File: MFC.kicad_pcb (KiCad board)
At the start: 2 copper layers, 101.6 x 53.3 mm, 39 parts, among them J1 DA15_Receptacle_MountingHoles, J12 Conn_01x01_Pin, J2 Conn_01x04_Pin, J3 Conn_01x03_Socket, J4 647676-3, J5 Conn_01x03_Pin, J6 Conn_01x03_Pin, U1 MAX232

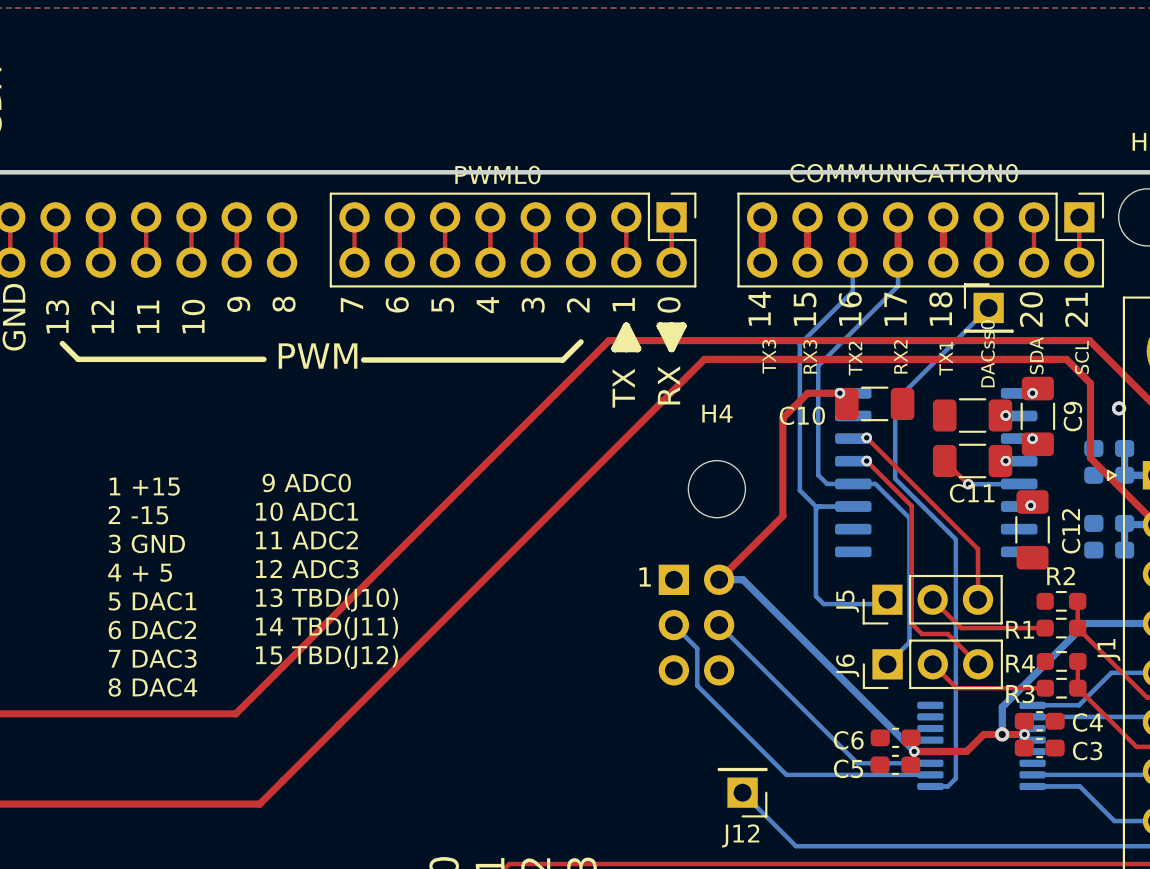
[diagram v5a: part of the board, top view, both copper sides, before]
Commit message: Added choice for serial com
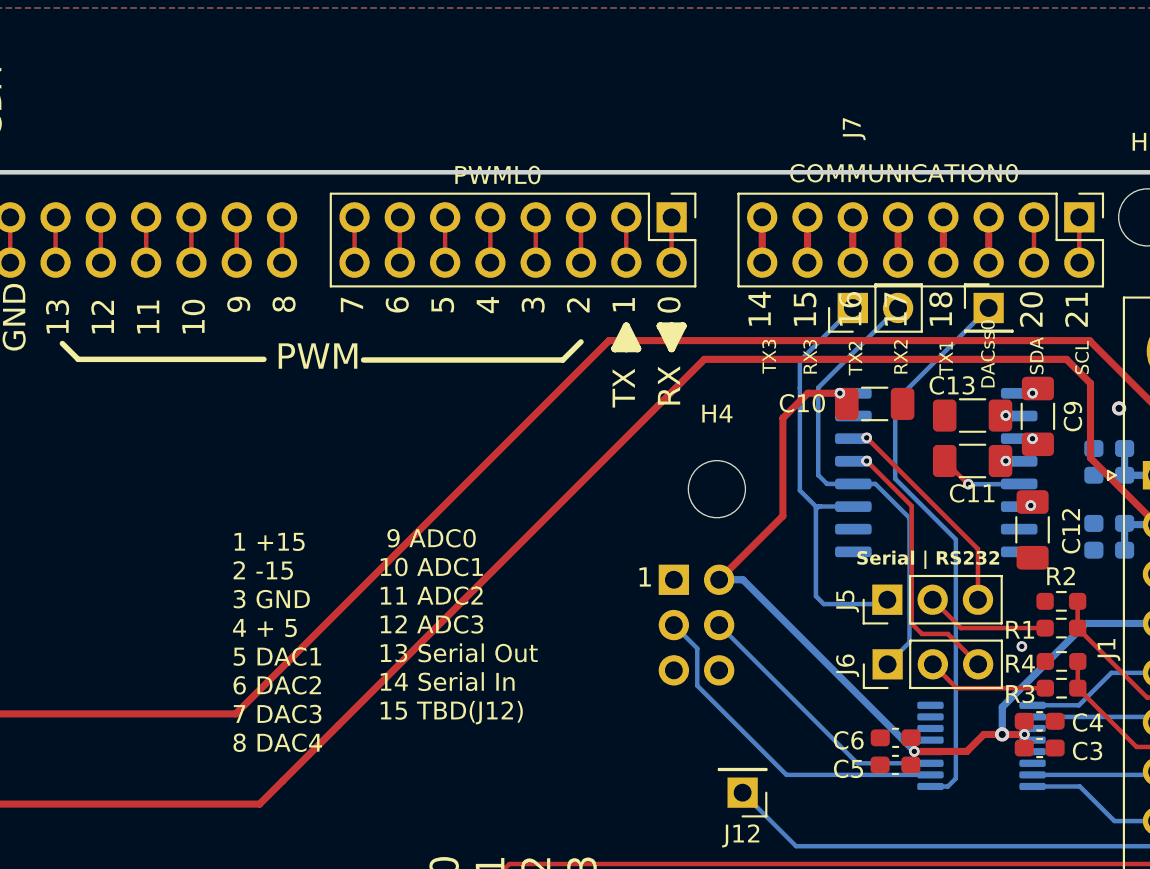
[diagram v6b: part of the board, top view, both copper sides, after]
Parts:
- added J7: Conn_01x02_Pin, Connector_PinHeader_2.54mm:PinHeader_1x02_P2.54mm_Vertical, F.Cu at (160.7, 76.8)
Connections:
- J5 pad 1: /TXD2 -> /TX2
- J6 pad 1: /RXD2 -> /RX2
- U1 pad 11: /TXD2 -> /TX2
- U1 pad 12: /RXD2 -> /RX2
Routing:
- net /RXD2: track 31.1 -> 2.54 mm
- net /TXD2: track 29.5 -> 2.54 mm
- net /RX2: track 0.00 -> 26.1 mm
- net /TX2: track 0.00 -> 24.5 mm
- net GND: vias 3 -> 4
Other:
- board text added: "9 ADC0 10 ADC1 11 ADC2 12 ADC3 13 Serial Out 14 Serial In 15 TBD(J12)"
- board text added: "Serial | RS232"
- board text removed: "9 ADC0 10 ADC1 11 ADC2 12 ADC3 13 TBD(J10) 14 TBD(J11) 15 TBD(J12)"

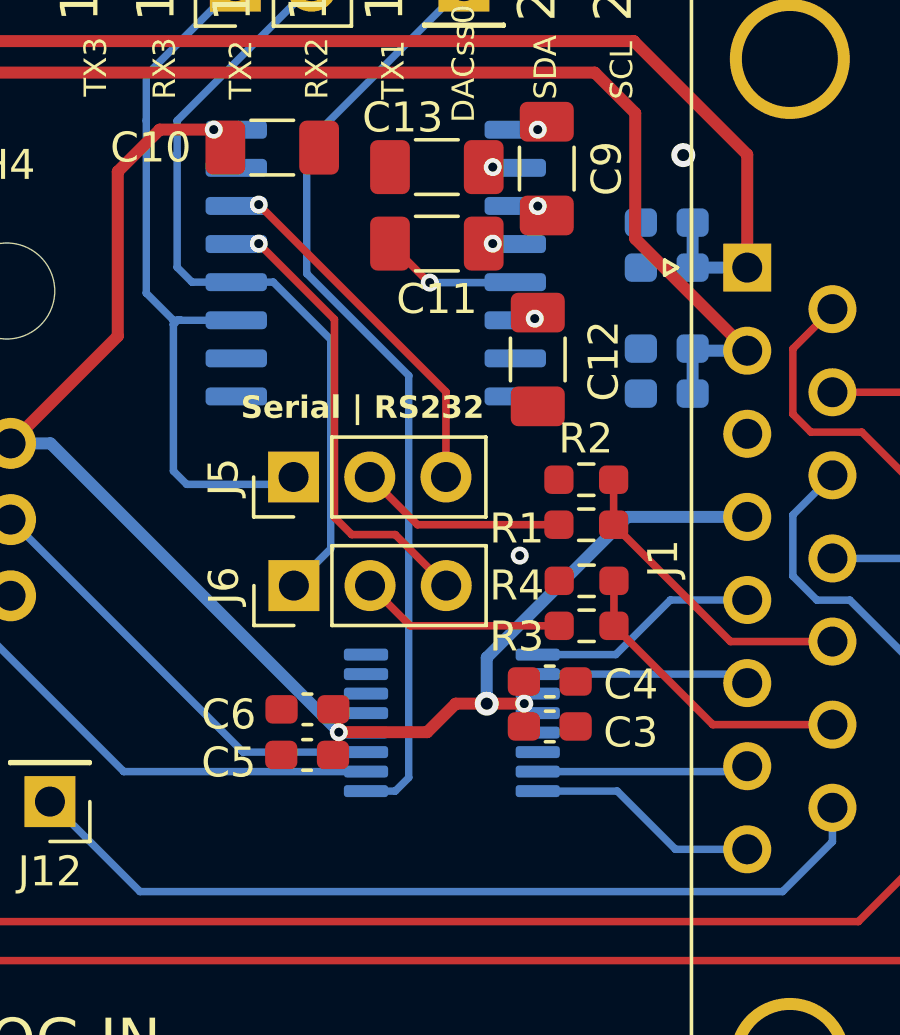
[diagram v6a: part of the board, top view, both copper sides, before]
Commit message: Update 10u capa for tantal
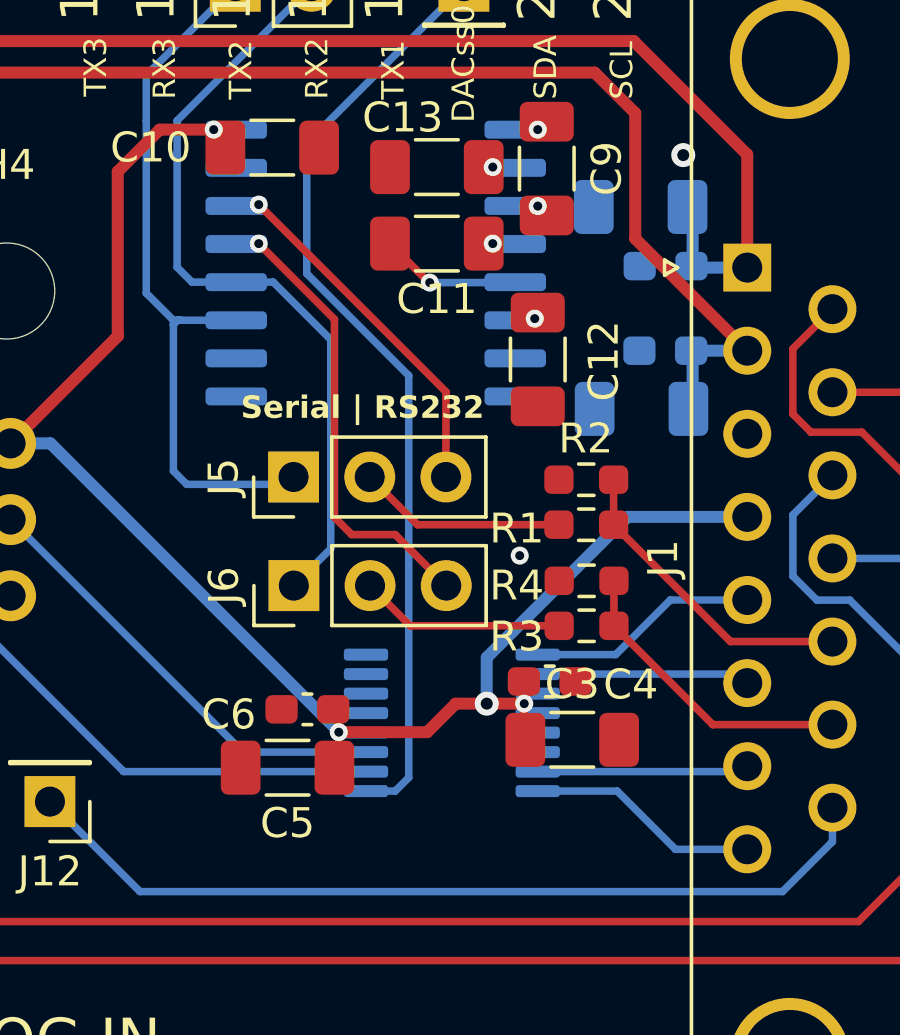
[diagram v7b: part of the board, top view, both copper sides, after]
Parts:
- C1, C3, C5, C7: footprint Capacitor_SMD:C_0603_1608Metric_Pad1.08x0.95mm_HandSolder -> Capacitor_SMD:C_1206_3216Metric_Pad1.33x1.80mm_HandSolder
- moved C1 2.20 mm to (174.2, 84.2)
- moved C7 2.18 mm to (174.3, 90.9)
- moved C2 1.45 mm to (175.1, 86.2)
- moved C8 1.43 mm to (175.1, 89.0)
- moved C3 0.87 mm to (171.9, 101.9)
- moved C5 0.78 mm to (162.5, 102.9)

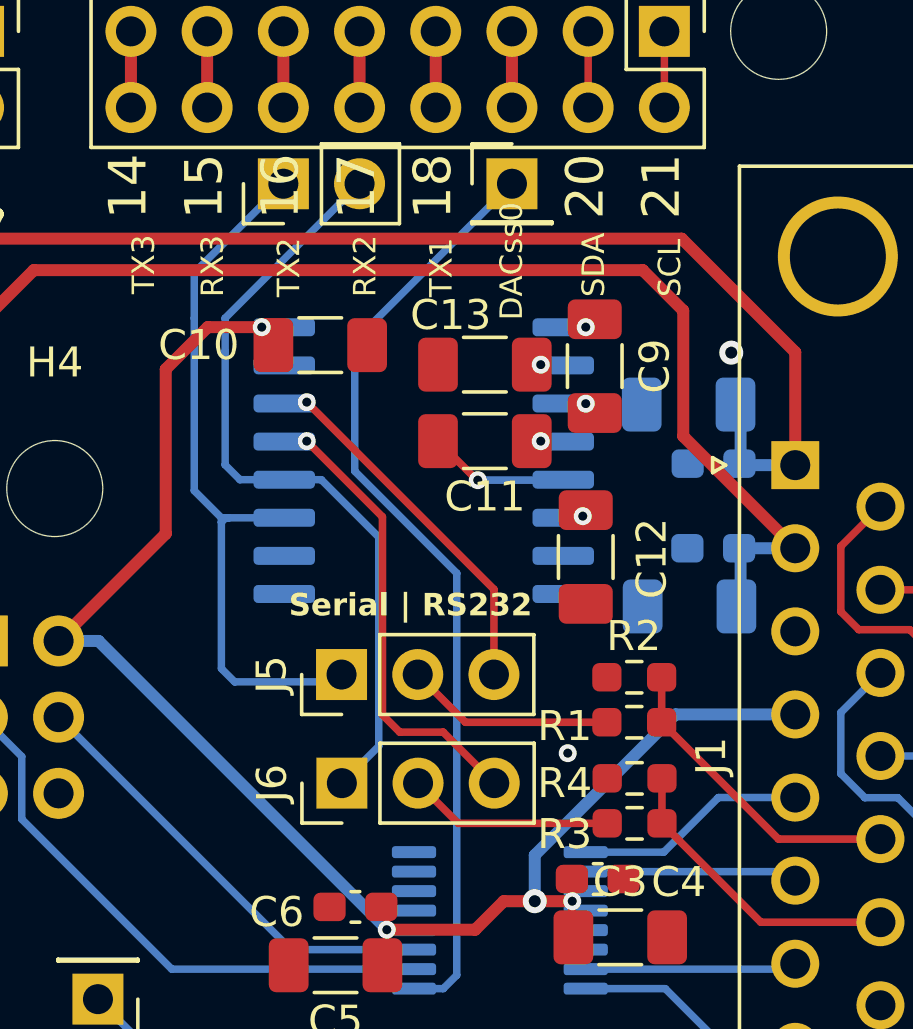
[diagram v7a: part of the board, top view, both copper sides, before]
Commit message: Minor change for better ground coverage
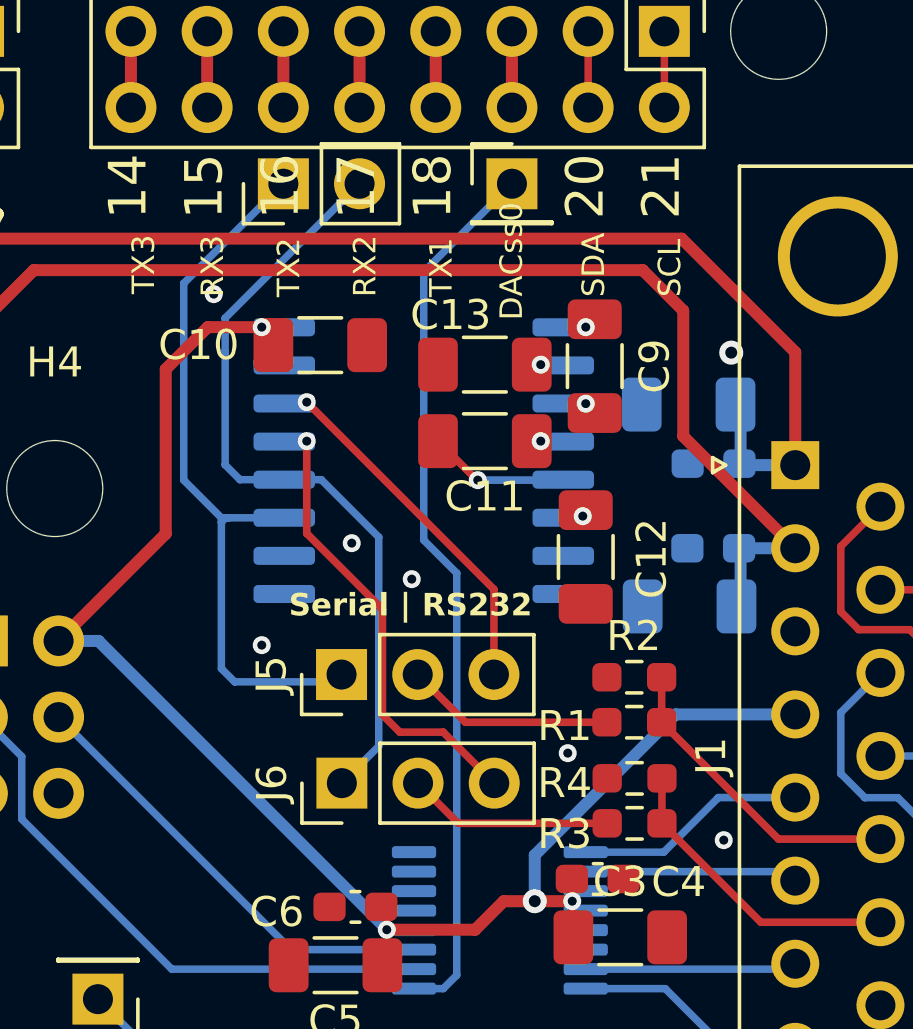
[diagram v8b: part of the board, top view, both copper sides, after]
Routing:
- net /SS: track 31.6 -> 29.7 mm
- net GND: vias 4 -> 9
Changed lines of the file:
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@@
   )
   (segment (start 113.476 71.74) (end 113.476 74.28) (width 0.25) (layer "F.Cu") (net 1))
+  (via (at 163 88.8) (size 0.6) (drill 0.3) (layers "F.Cu" "B.Cu") (free) (net 1))
+  (via (at 165 90) (size 0.6) (drill 0.3) (layers "F.Cu" "B.Cu") (free) (net 1))
   (via (at 184.4 98.4) (size 0.8) (drill 0.4) (layers "F.Cu" "B.Cu") (free) (net 1))
   (via (at 149.9 113.9) (size 0.8) (drill 0.4) (layers "F.Cu" "B.Cu") (free) (net 1))
+  (via (at 160 92.2) (size 0.6) (drill 0.3) (layers "F.Cu" "B.Cu") (free) (net 1))
   (via (at 170.2 95.8) (size 0.6) (drill 0.3) (layers "F.Cu" "B.Cu") (free) (net 1))
+  (via (at 158.4 80.5) (size 0.6) (drill 0.3) (layers "F.Cu" "B.Cu") (free) (net 1))
   (via (at 175.65 82.45) (size 0.8) (drill 0.4) (layers "F.Cu" "B.Cu") (free) (net 1))
+  (via (at 175.4 98.7) (size 0.6) (drill 0.3) (layers "F.Cu" "B.Cu") (free) (net 1))
   (segment (start 160.72 120) (end 160.72 117.46) (width 0.25) (layer "F.Cu") (net 2))
   (segment (start 163.26 117.46) (end 163.26 120) (width 0.25) (layer "F.Cu") (net 3))
@@
   (segment (start 176.2 116) (end 181.5887 116) (width 0.25) (layer "B.Cu") (net 63))
   (segment (start 184.0137 95.895) (end 180.623369 95.895) (width 0.25) (layer "B.Cu") (net 63))
+  (segment (start 166.5 103.2) (end 166.05 103.65) (width 0.25) (layer "B.Cu") (net 64))
+  (segment (start 165.4 88.7) (end 166.5 89.8) (width 0.25) (layer "B.Cu") (net 64))
+  (segment (start 166.5 89.8) (end 166.5 103.2) (width 0.25) (layer "B.Cu") (net 64))
   (segment (start 166.05 103.65) (end 165.075 103.65) (width 0.25) (layer "B.Cu") (net 64))
-  (segment (start 168.34 76.82) (end 163.1 82.06) (width 0.25) (layer "B.Cu") (net 64))
-  (segment (start 166.5 103.2) (end 166.05 103.65) (width 0.25) (layer "B.Cu") (net 64))
-  (segment (start 166.5 89.8) (end 166.5 103.2) (width 0.25) (layer "B.Cu") (net 64))
-  (segment (start 163.1 82.06) (end 163.1 86.4) (width 0.25) (layer "B.Cu") (net 64))
-  (segment (start 163.1 86.4) (end 166.5 89.8) (width 0.25) (layer "B.Cu") (net 64))
+  (segment (start 165.4 79.76) (end 165.4 88.7) (width 0.25) (layer "B.Cu") (net 64))
+  (segment (start 168.34 76.82) (end 165.4 79.76) (width 0.25) (layer "B.Cu") (net 64))
   (segment (start 122.62 117.46) (end 122.62 120) (width 0.4) (layer "F.Cu") (net 65))
   (via (at 169.3 85.4) (size 0.6) (drill 0.3) (layers "F.Cu" "B.Cu") (net 66))
@@
   (segment (start 167.74 90.34) (end 167.74 93.18) (width 0.254) (layer "F.Cu") (net 72))
   (via (at 161.5 84.1) (size 0.6) (drill 0.3) (layers "F.Cu" "B.Cu") (net 72))
+  (segment (start 164.023 91) (end 161.5 88.477) (width 0.254) (layer "F.Cu") (net 73))
+  (segment (start 164.023 91) (end 164.023 94.523) (width 0.254) (layer "F.Cu") (net 73))
   (segment (start 166.05 95.1) (end 167.75 96.8) (width 0.254) (layer "F.Cu") (net 73))
-  (segment (start 161.5 85.4) (end 164.023 87.923) (width 0.254) (layer "F.Cu") (net 73))
-  (segment (start 164.023 87.923) (end 164.023 94.523) (width 0.254) (layer "F.Cu") (net 73))
+  (segment (start 161.5 88.477) (end 161.5 85.4) (width 0.254) (layer "F.Cu") (net 73))
   (segment (start 164.6 95.1) (end 166.05 95.1) (width 0.254) (layer "F.Cu") (net 73))
   (segment (start 164.023 94.523) (end 164.6 95.1) (width 0.254) (layer "F.Cu") (net 73))
@@
   (segment (start 166.55 98.14) (end 171.515 98.14) (width 0.254) (layer "F.Cu") (net 79))
   (segment (start 165.21 96.8) (end 166.55 98.14) (width 0.254) (layer "F.Cu") (net 79))
-  (segment (start 157.75 81.3) (end 157.75 87.05) (width 0.25) (layer "B.Cu") (net 80))
-  (segment (start 157.75 79.79) (end 157.75 81.3) (width 0.25) (layer "B.Cu") (net 80))
   (segment (start 158.655 88.1) (end 158.655 92.980305) (width 0.25) (layer "B.Cu") (net 80))
+  (segment (start 160.72 76.82) (end 157.4 80.14) (width 0.25) (layer "B.Cu") (net 80))
   (segment (start 158.655 92.980305) (end 159.099695 93.425) (width 0.25) (layer "B.Cu") (net 80))
-  (segment (start 160.72 76.82) (end 157.75 79.79) (width 0.25) (layer "B.Cu") (net 80))
+  (segment (start 157.4 86.7) (end 158.655 87.955) (width 0.25) (layer "B.Cu") (net 80))
   (segment (start 158.9 87.955) (end 160.75 87.955) (width 0.25) (layer "B.Cu") (net 80))
   (segment (start 162.415 93.425) (end 162.66 93.18) (width 0.25) (layer "B.Cu") (net 80))
   (segment (start 159.099695 93.425) (end 162.415 93.425) (width 0.25) (layer "B.Cu") (net 80))
-  (segment (start 157.75 87.05) (end 158.655 87.955) (width 0.25) (layer "B.Cu") (net 80))
   (segment (start 158.8 87.955) (end 158.655 88.1) (width 0.25) (layer "B.Cu") (net 80))
   (segment (start 158.9 87.955) (end 158.8 87.955) (width 0.25) (layer "B.Cu") (net 80))
   (segment (start 158.655 87.955) (end 158.655 88.1) (width 0.25) (layer "B.Cu") (net 80))
+  (segment (start 157.4 80.14) (end 157.4 86.7) (width 0.25) (layer "B.Cu") (net 80))
   (segment (start 158.655 87.955) (end 158.9 87.955) (width 0.25) (layer "B.Cu") (net 80))
   (segment (start 158.78 86.19) (end 159.275 86.685) (width 0.25) (layer "B.Cu") (net 81))
